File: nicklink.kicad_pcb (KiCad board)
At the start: 2 copper layers, 34 x 25.5 mm, 46 parts, among them J1 Conn_02x10_Odd_Even, J2 USB_C_Receptacle_USB2.0_16P, J3 Conn_02x10_Odd_Even, Q1 DMP2165UW, SW1 RESET, SW2 BOOT0, U1 STM32F103C8T6, U2 TLV75533PDRV, U3 USBLC6-2P6, U4 LSM6DSV16X, Y1 8MHz

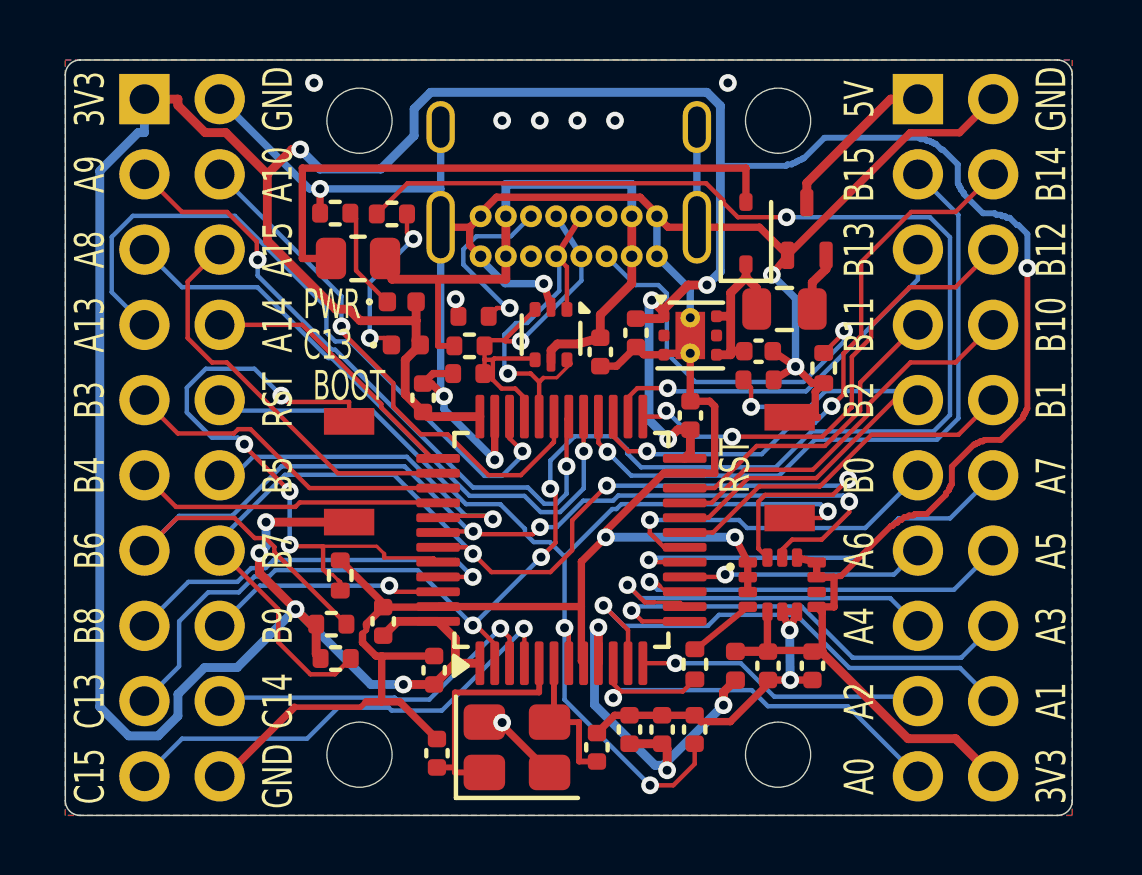
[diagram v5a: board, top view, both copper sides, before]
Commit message: v1.3 second review wave: TLV76733 LDO, VBUS_D off the USB shell, IMU spacing, firmware fixes
Five reviewers (power C+, MCU B, USB B, IMU/GPIO B+, fab B+); all must-fixes done:
- U2 TLV75533 -> TLV76733DRVR (same DRV0006A pads, VIN/EN 18 V): J1.1 hot-plug
  rang VSYS past the TLV755's 6 V abs max. SNS->OUT, pin 5->GND stubs. C12 16 V.
  New SPICE bench 12 (J1.1 hot-plug, 1.5-3 uH USB cables).
- VBUS_D hops to B.Cu under the USB4085 shell; F.Cu keep-out over its GND dimples.
- IMU: pour keep-out off the GND pads, bottom GND via outside the body.
- Net classes: signals 0.127/0.127 mm, GND and new Rail class (3V3) 0.2 mm; seed 3
  now routes 100% with Freerouting alone. DRC 0/0/0, ERC 0/0, one GND cluster,
  no via within 0.1 mm of an SMD pad.
- Tools: stitch.py keeps vias off SMD pads; fixroute.py via/screw keep-outs and
  path smoothing; autoroute RIPUP=1 second pass; swapfp.py.
- Firmware: VTOR, clock bring-up from any state, CSS/NMI fallback, PVD 2.9 V,
  standby (WKUP) and adc commands, pin-map test fixed: Renode 10/10.
- Docs: 5V-pin output/short behaviour, battery caveat, PC13-15 shared 3 mA,
  I2C1/SPI1 remap conflicts (ES096), review write-up in docs/REVIEW.md.

Co-Authored-By: Claude Opus 5.5 <noreply@anthropic.com>
Claude-Session: https://claude.ai/code/session_01KPMtzubqGeBFaq48UcVZaf
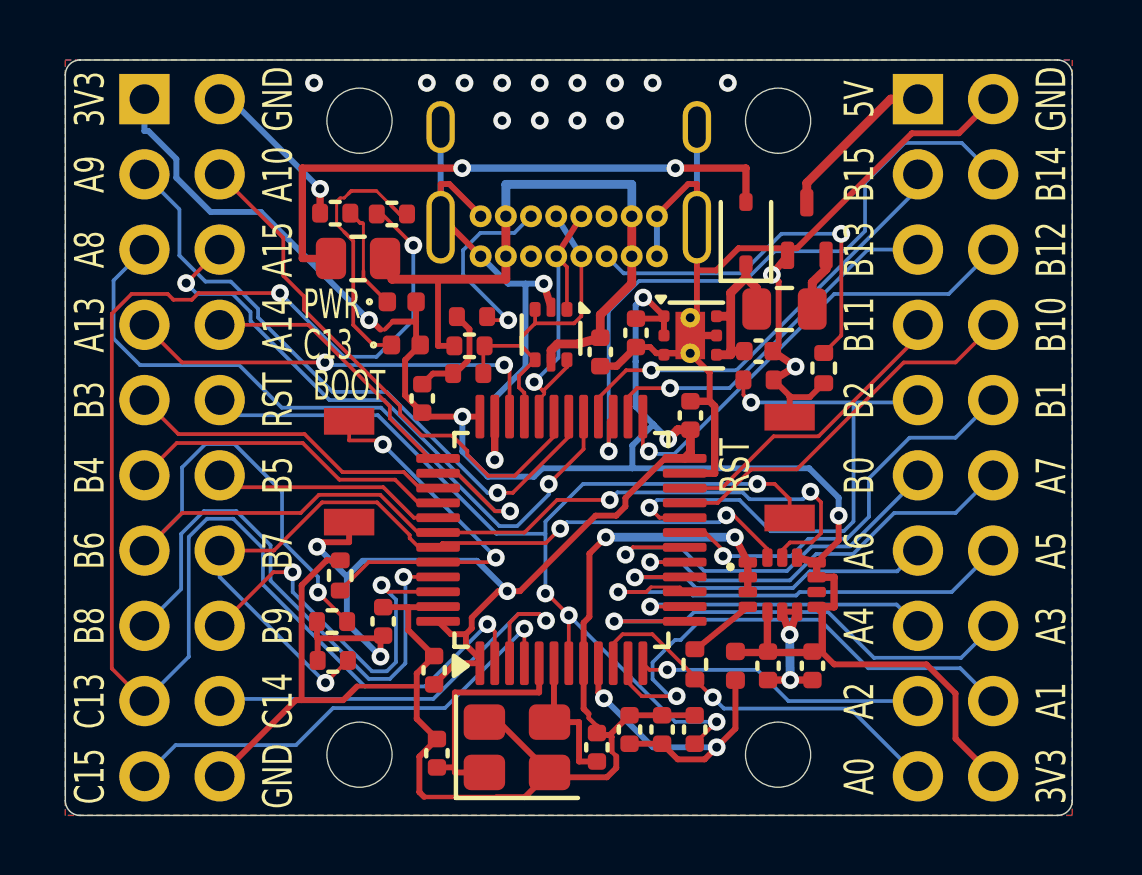
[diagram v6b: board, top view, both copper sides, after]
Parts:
- C12: value 4u7 -> 4u7 16V
- U2: value TLV75533PDRV -> TLV76733DRVR
- moved R9 0.12 mm to (109.0, 120.3)
- moved R7 0.09 mm to (109.0, 119.0)
- moved R5 0.05 mm to (113.7, 108.7)
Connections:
- U2 pad 2: unconnected-(U2-NC-Pad2) -> +3.3V
- U2 pad 5: unconnected-(U2-NC-Pad5) -> GND
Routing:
- net +3.3V: track 150.0 -> 97.4 mm, vias 9 -> 8
- net /PC13: track 64.7 -> 51.6 mm, vias 4 -> 3
- net /PB7: track 39.4 -> 28.1 mm
- net /PA13: track 23.5 -> 14.5 mm, vias 1 -> 2
- net /BOOT0: track 21.3 -> 12.9 mm, vias 4 -> 2
- net /PB15: track 23.1 -> 14.8 mm
- net /PB8: track 13.4 -> 18.9 mm
- net /PB9: track 8.02 -> 13.4 mm, vias 1 -> 2
- net /PA15: track 13.8 -> 18.9 mm, vias 0 -> 2
- net /PB5: track 12.3 -> 7.96 mm, vias 1 -> 0
- net /PA6: track 8.24 -> 11.9 mm
- net /PC14: track 11.8 -> 15.1 mm
- net /USER_LED_K: track 5.71 -> 8.81 mm, vias 2 -> 0
- net /PA8: track 21.3 -> 24.3 mm
- net /PB2: track 16.5 -> 19.4 mm, vias 1 -> 2
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
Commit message: JLC order fixes: LSM6DSV IMU, THT by JLC, one-line-per-part BOM, Gerber-frame CPL
Placing the first real JLCPCB Economic PCBA order for v1.3 turned up
problems that DRC and the review waves didn't catch. Copper is unchanged
(Gerbers regenerate identical apart from timestamps).

- U4: LSM6DSV16X (C5267406) -> LSM6DSV (C41785564). JLC lists the
  LSM6DSV16X as "Standard PCBA only" (X-ray); the LSM6DSV is allowed on
  Economic. Same LGA-14 pinout and I2C wiring, same registers for
  everything the firmware and SFLP use, WHO_AM_I 0x70. It lacks the MLC,
  Qvar and analog hub, none of which the board uses. Project symbol
  renamed; board/schematic fields updated (DRC parity 0).
- J1/J3 get LCSC C5383109 (HanElectricity 2541WV-2x10P) and J1-J3 are
  assembled by JLC instead of hand-soldered.
- fab.sh BOM: grouped by LCSC number, so JLC no longer unselects
  R1/R8/R10, R4/R5, R7/R9/R11 and SW1/SW2 as "multiple lines matched to
  the same part"; THT parts included.
- fab.sh CPL: written in the Gerber frame (JLC flagged every part as
  offset from the board with the old lower-left origin); rotation and
  origin corrections keyed by LCSC part, including the header (-90,
  centred) and USB4085 origin; asserts every part lands on the board.
- Docs: README (IMU, ordering: ENIG needs green on Economic, avoid black
  mask for the 0.11 mm USB-C pad gaps), REVIEW.md "JLC order round",
  parts/IMU research, firmware strings. Renode tests 10/10.

Co-Authored-By: Claude Opus 5.5 <noreply@anthropic.com>
Claude-Session: https://claude.ai/code/session_017LucoBJmh2YFvzHpYSamwe
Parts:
- U4: value LSM6DSV16X -> LSM6DSV
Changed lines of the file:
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@@
 			)
 		)
-		(property "Value" "LSM6DSV16X"
+		(property "Value" "LSM6DSV"
 			(at 0 2.2 0)
 			(layer "F.Fab")
@@
 			)
 		)
-		(property "Datasheet" "https://www.st.com/resource/en/datasheet/lsm6dsv16x.pdf"
+		(property "Datasheet" "https://www.st.com/resource/en/datasheet/lsm6dsv.pdf"
 			(at 0 0 0)
 			(layer "F.Fab")
@@
 			)
 		)
-		(property "MPN" "ST LSM6DSV16XTR"
+		(property "MPN" "ST LSM6DSV (JLC: LSM6DSVETR)"
 			(at 0 0 0)
 			(layer "F.Fab")
@@
 			)
 		)
-		(property "LCSC" "C5267406"
+		(property "LCSC" "C41785564"
 			(at 0 0 0)
 			(layer "F.Fab")
@@
 			)
 		)
+		(property "MPN" "HanElectricity 2541WV-2x10P (male, 6 mm pins, 3 mm tail)"
+			(at 0 0 180)
+			(layer "F.Fab")
+			(hide yes)
+			(effects
+				(font
+					(size 1.27 1.27)
+					(thickness 0.15)
+				)
+			)
+		)
+		(property "LCSC" "C5383109"
+			(at 0 0 180)
+			(layer "F.Fab")
+			(hide yes)
+			(effects
+				(font
+					(size 1.27 1.27)
+					(thickness 0.15)
+				)
+			)
+		)
 		(attr through_hole)
 		(duplicate_pad_numbers_are_jumpers no)
@@
 					(thickness 0.15)
 				)
+			)
+		)
+		(property "MPN" "HanElectricity 2541WV-2x10P (male, 6 mm pins, 3 mm tail)"
+			(at 0 0 180)
+			(layer "F.Fab")
+			(hide yes)
+			(effects
+				(font
+					(size 1.27 1.27)
+					(thickness 0.15)
+				)
+			)
+		)
+		(property "LCSC" "C5383109"
+			(at 0 0 180)
+			(layer "F.Fab")
+			(hide yes)
+			(effects
+				(font
+					(size 1.27 1.27)
+					(thickness 0.15)
+				)
